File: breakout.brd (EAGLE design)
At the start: 44.5 x 25.4 mm, 21 parts

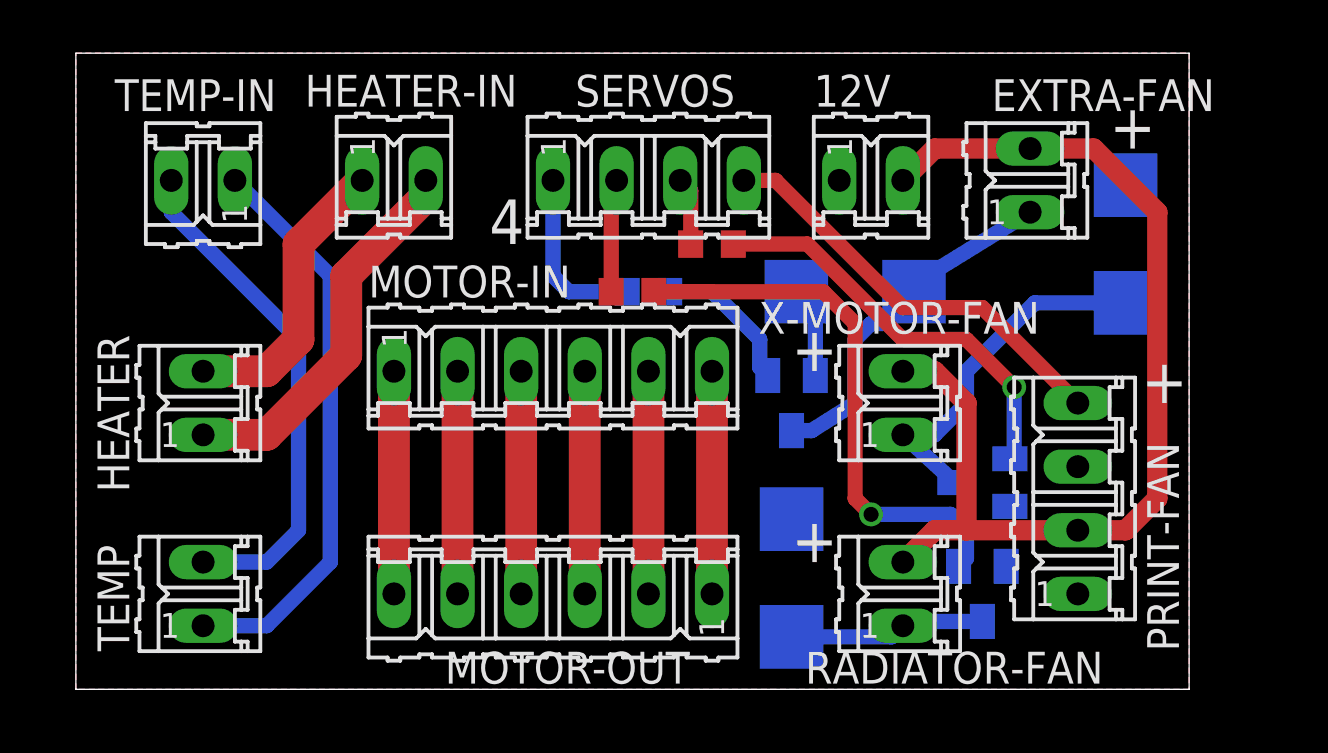
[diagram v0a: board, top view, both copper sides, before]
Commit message: Adjusted to 2mm spacing for motor connector, and moved some connectors a bit.
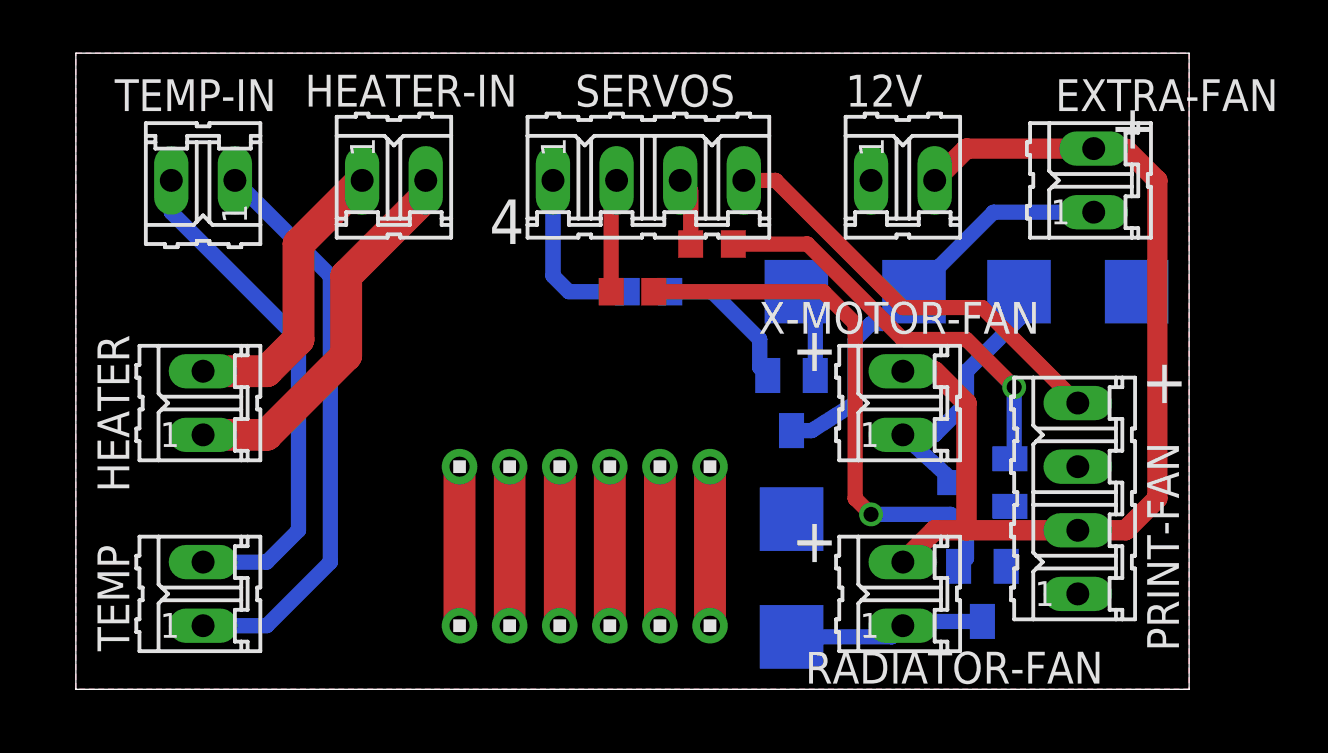
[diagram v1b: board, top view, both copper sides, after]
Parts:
- removed MOTOR-IN, MOTOR-OUT: (no value), con-amp-quick:06P
- added U$1, U$2: 1X6, headers(2mm):1X6
- moved D2 2.69 mm to (45.1, 15.9), turned to 180 degrees
- moved EXTRA-FAN 2.54 mm to (45.7, 20.3)
- moved 12V 1.27 mm to (38.1, 20.3)
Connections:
- net N$1: now also U$1.1, U$2.6; no longer MOTOR-IN.1, MOTOR-OUT.6
- net N$2: now also U$1.2, U$2.5; no longer MOTOR-IN.2, MOTOR-OUT.5
- net N$3: now also U$1.3, U$2.4; no longer MOTOR-IN.3, MOTOR-OUT.4
- net N$4: now also U$1.4, U$2.3; no longer MOTOR-IN.4, MOTOR-OUT.3
- net N$5: now also U$1.5, U$2.2; no longer MOTOR-IN.5, MOTOR-OUT.2
- net N$6: now also U$1.6, U$2.1; no longer MOTOR-IN.6, MOTOR-OUT.1
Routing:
- net N$13: track 14.2 -> 18.2 mm
- net N$16: track 14.6 -> 11.2 mm
- net N$6: track 8.89 -> 6.35 mm
- net N$5: track 8.89 -> 6.35 mm
- net N$4: track 8.89 -> 6.35 mm
- net N$3: track 8.89 -> 6.35 mm
- net N$2: track 8.89 -> 6.35 mm
- net N$1: track 8.89 -> 6.35 mm
- net +12V: track 42.5 -> 42.0 mm

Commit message: Adjusting labels and positioning.
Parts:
- renumbered EXTRA-FAN to FAN
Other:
- board text added: "GND"
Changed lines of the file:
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@@
 <text x="33.655" y="5.08" size="1.778" layer="25">+</text>
 <text x="33.655" y="12.7" size="1.778" layer="25">+</text>
-<text x="46.355" y="21.59" size="1.778" layer="25">+</text>
+<text x="47.625" y="21.59" size="1.778" layer="25">+</text>
 <text x="47.625" y="11.43" size="1.778" layer="25">+</text>
 <text x="21.59" y="17.78" size="1.778" layer="25">4</text>
+<text x="40.005" y="22.86" size="1.778" layer="25">+</text>
+<text x="35.56" y="22.86" size="0.6096" layer="25" rot="R90">GND</text>
 </plain>
 <attributes>
@@
 <attribute name="VALUE" x="38.735" y="13.589" size="0.4064" layer="28" font="vector" rot="MR0"/>
 </element>
-<element name="EXTRA-FAN" library="con-amp-quick" package="02P" value="" x="45.72" y="20.32" smashed="yes" rot="R90">
+<element name="FAN" library="con-amp-quick" package="02P" value="" x="45.72" y="20.32" smashed="yes" rot="R90">
 <attribute name="MF" value="" x="45.72" y="20.32" size="1.778" layer="27" rot="R90" display="off"/>
 <attribute name="MPN" value="" x="45.72" y="20.32" size="1.778" layer="27" rot="R90" display="off"/>
-<attribute name="NAME" x="53.086" y="24.3586" size="1.27" layer="25" ratio="10" rot="R180"/>
+<attribute name="NAME" x="48.006" y="24.3586" size="1.27" layer="25" ratio="10" rot="R180"/>
 <attribute name="OC_FARNELL" value="unknown" x="45.72" y="20.32" size="1.778" layer="27" rot="R90" display="off"/>
 <attribute name="OC_NEWARK" value="unknown" x="45.72" y="20.32" size="1.778" layer="27" rot="R90" display="off"/>
@@
 <attribute name="VALUE" x="41.9354" y="9.144" size="1.27" layer="27" ratio="10" rot="R90"/>
 </element>
-<element name="12V" library="con-amp-quick" package="02P" value="" x="38.1" y="20.32">
+<element name="12V" library="con-amp-quick" package="02P" value="" x="38.1" y="20.32" smashed="yes">
 <attribute name="MF" value="" x="38.1" y="20.32" size="1.778" layer="27" display="off"/>
 <attribute name="MPN" value="" x="38.1" y="20.32" size="1.778" layer="27" display="off"/>
+<attribute name="NAME" x="36.449" y="23.2664" size="1.27" layer="25" ratio="10"/>
 <attribute name="OC_FARNELL" value="unknown" x="38.1" y="20.32" size="1.778" layer="27" display="off"/>
 <attribute name="OC_NEWARK" value="unknown" x="38.1" y="20.32" size="1.778" layer="27" display="off"/>
+<attribute name="VALUE" x="35.814" y="16.4846" size="1.27" layer="27" ratio="10"/>
 </element>
 <element name="U$1" library="headers(2mm)" package="1X6" value="1X6" x="25.4" y="2.54"/>
@@
 <contactref element="RADIATOR-FAN" pad="2"/>
 <contactref element="X-MOTOR-FAN" pad="2"/>
-<contactref element="EXTRA-FAN" pad="2"/>
+<contactref element="FAN" pad="2"/>
 <wire x1="48.26" y1="7.62" x2="48.26" y2="20.32" width="0.8128" layer="1"/>
 <wire x1="48.26" y1="7.62" x2="46.99" y2="6.35" width="0.8128" layer="1"/>
@@
 <signal name="N$13">
 <contactref element="D3" pad="C"/>
-<contactref element="EXTRA-FAN" pad="1"/>
+<contactref element="FAN" pad="1"/>
 <contactref element="T3" pad="C"/>
 <wire x1="33.655" y1="10.33" x2="34.46" y2="10.33" width="0.6096" layer="16"/>
